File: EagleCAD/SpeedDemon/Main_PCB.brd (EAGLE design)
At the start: 77 x 46.5 mm, 71 parts, among them Q1 DMC2700, U3 LM3676, U4 STM32F072-LQFP48, X1 32.768kHz

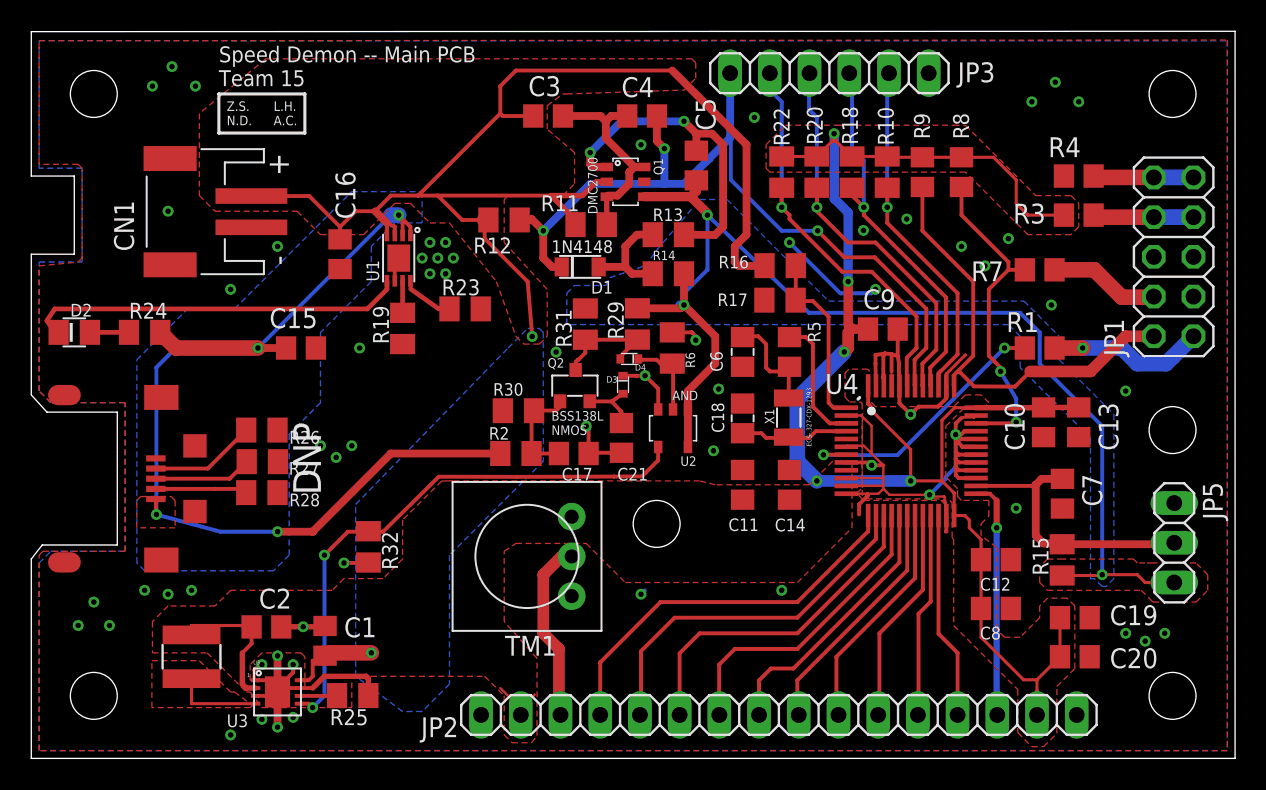
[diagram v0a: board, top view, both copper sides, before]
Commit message: added 8MHz oscillator citcuit to layout and schematic
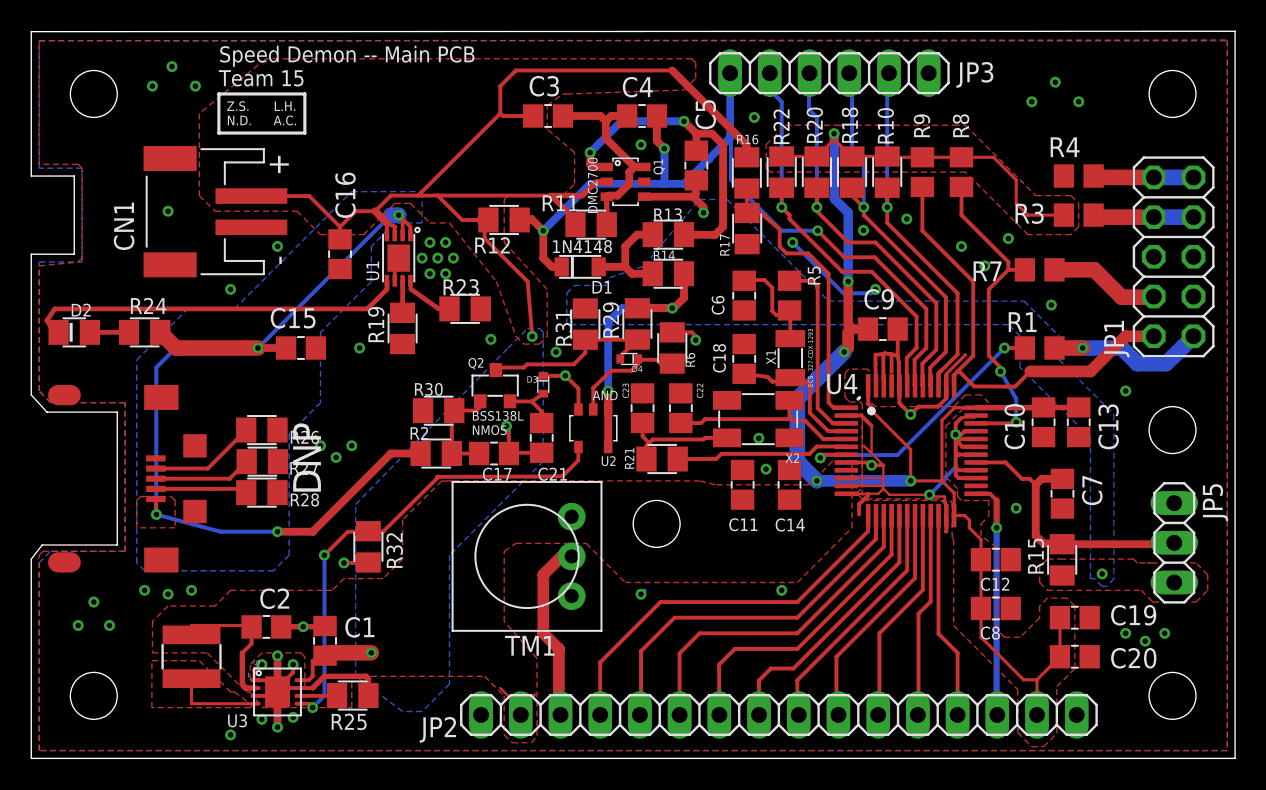
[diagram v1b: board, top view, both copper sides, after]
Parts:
- added C22, C23: 22pF, LCRD_SMD_generics:C_0805
- added R21: 0, LCRD_SMD_generics:R_0805
- added X2: (no value), LCRD_SMD_generics:4-SMD
- moved R16 6.30 mm to (45.8, 37.5), turned to 90 degrees
- moved Q2 5.10 mm to (29.7, 23.8)
- moved C17 5.10 mm to (29.6, 19.5)
- moved C21 5.10 mm to (32.6, 20.5)
- moved D3 5.10 mm to (32.8, 23.9)
- moved R2 5.10 mm to (25.9, 19.5)
- moved R30 5.10 mm to (26.1, 22.2)
- moved U2 5.10 mm to (36.0, 21.1)
- moved R17 5.04 mm to (45.8, 33.9), turned to 90 degrees
- moved C18 3.80 mm to (45.6, 25.6)
- moved X1 3.80 mm to (48.5, 25.6)
- moved C6 3.60 mm to (45.6, 29.6)
- moved R5 3.60 mm to (48.5, 29.6)
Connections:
- new net N$13: R21.2, U4.6
- new net N$17: C22.2, U4.5, X2.P$01
- new net N$18: C23.2, R21.1, X2.P$03
- net GND: now also C22.1, C23.1, U4.26, X2.P$02, X2.P$04; no longer U4.29, U4.5, U4.6
- net SENSOR_SIG_OP: now also U4.29; no longer U4.26
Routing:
- net VBATT+_SW: track 76.9 -> 22.9 mm, vias 3 -> 4
- net N$17: track 0.00 -> 12.5 mm
- net N$13: track 0.00 -> 11.1 mm
- net VBATT+: track 88.7 -> 79.7 mm
- net N$18: track 0.00 -> 7.66 mm
- net N$7: track 11.5 -> 18.7 mm
- net +V+_CHG: track 65.7 -> 60.6 mm
- net BATT_CHG_LOGIC_OP: track 35.7 -> 30.8 mm
- net N$28: track 7.23 -> 12.0 mm
- net N$5: track 8.26 -> 12.0 mm
- net GND: track 105.1 -> 102.4 mm, vias 62 -> 63
- net OSC32_OUT: track 7.00 -> 9.28 mm
- net N$11: track 5.25 -> 7.50 mm
- net SENSOR_SIG_OP: track 18.1 -> 18.7 mm
- net FL_RESET: track 17.2 -> 17.8 mm

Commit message: schematic/layout detail work.
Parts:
- CONN1: device USB_jack_102-4008-1-ND:UJ2-MIBH-4-MSMT-TR -> USB_micro_jack:USB_JACK_102-4008-1-ND_UJ2-MIBH-4-MSMT-TR
- Q2: value (none) -> BSS138L
- U2: value (none) -> NC7S08M
- moved C16 0.50 mm to (19.8, 32.8)
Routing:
- net GND: track 102.4 -> 85.4 mm, vias 63 -> 60
- net +3V3: track 114.3 -> 107.4 mm
- net PWR_SW: track 52.2 -> 50.3 mm
- net VBATT+: track 79.7 -> 78.4 mm
- net +V+_CHG: track 60.6 -> 59.6 mm
- net N$19: track 12.0 -> 12.8 mm
- net N$20: track 3.91 -> 4.49 mm
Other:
- outline, holes or cut-outs redrawn
- board text added: "L1"
- board text added: "Speed Demon -- Main PCB Team 15 (Rev.1)"
- board text removed: "Speed Demon -- Main PCB Team 15"
- board text removed: "U1"
- board text removed: "U3"

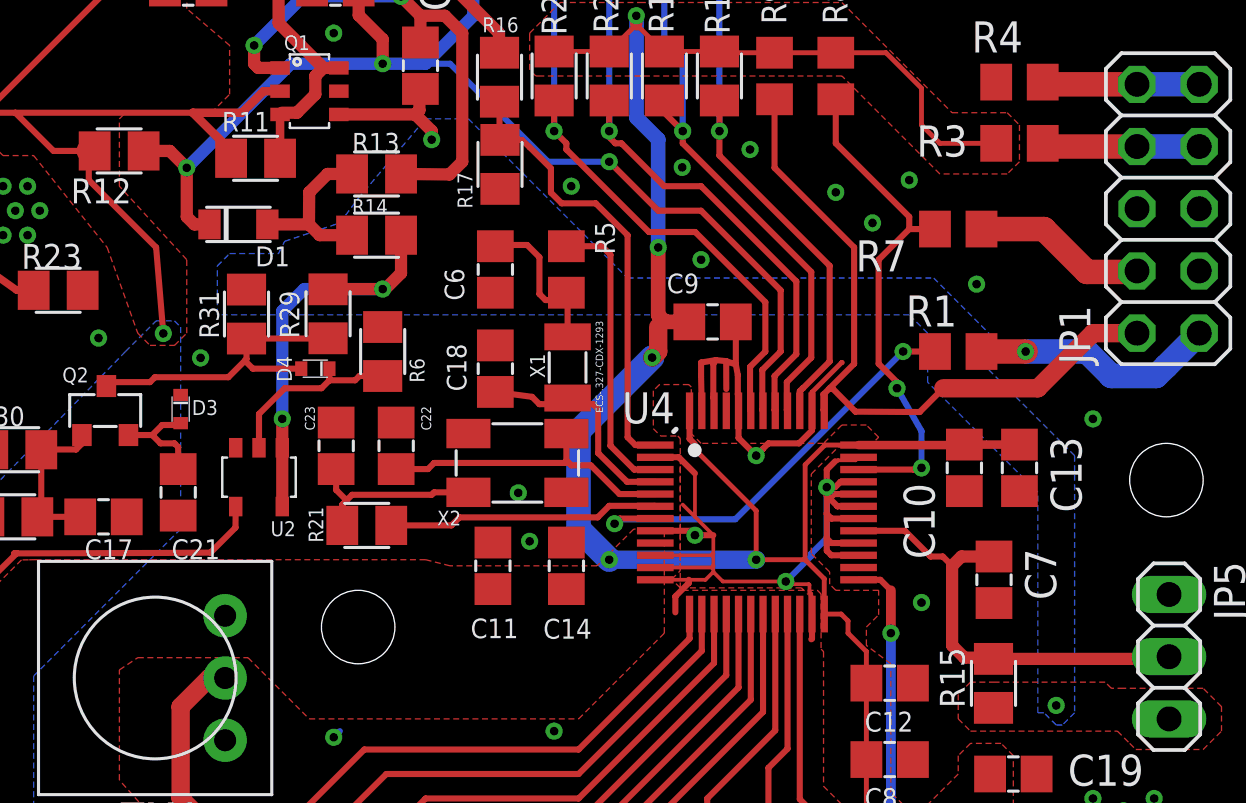
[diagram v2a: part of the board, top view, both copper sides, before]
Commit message: final changes to power defeat logic
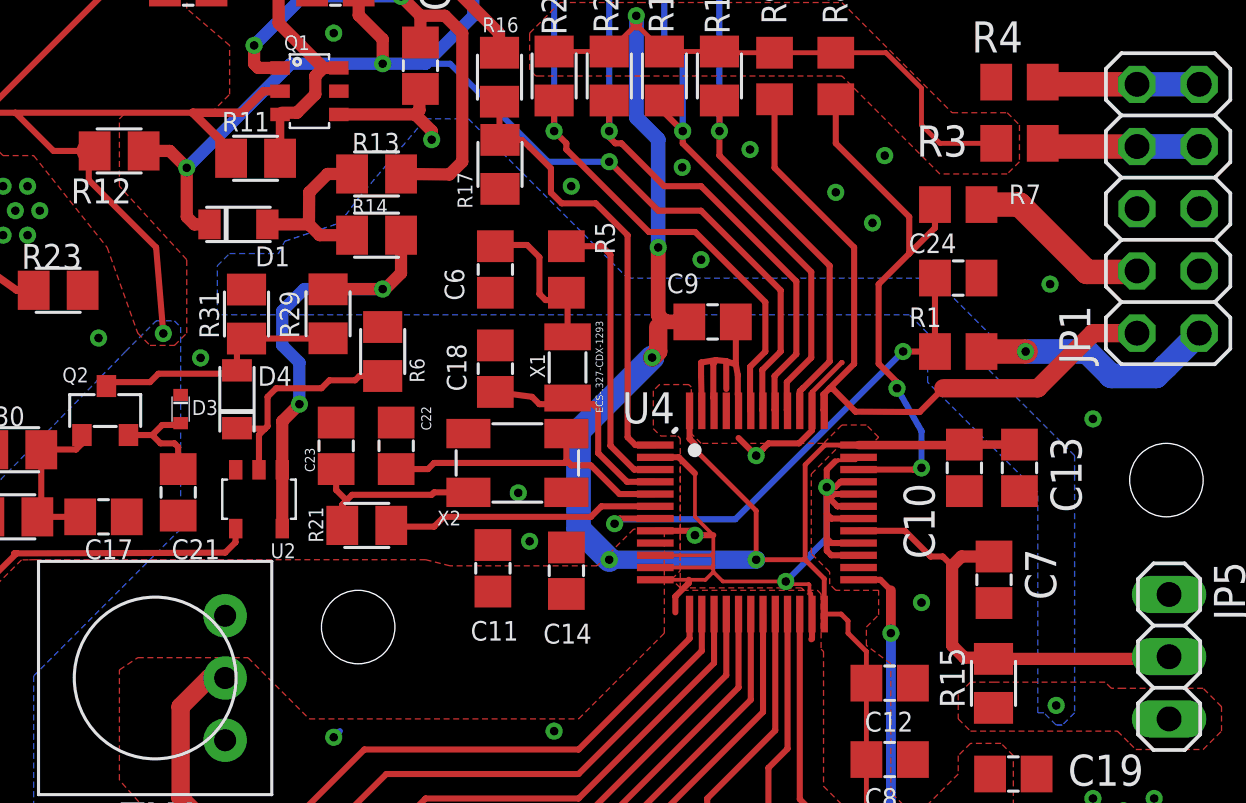
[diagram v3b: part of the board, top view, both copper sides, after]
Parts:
- added C24: 100nF, 0805_generics:C_0805
- D4: value (none) -> 1N4148; device LCRD_SMD_generics:SOD-882 -> LCRD_SMD_generics:D_SOD_123
- R31: value 1M -> DNP
- R6: value 1k -> 100k
- moved D4 3.44 mm to (35.0, 24.3), turned to 270 degrees
- moved R7 1.00 mm to (64.5, 32.2)
- moved U2 0.90 mm to (36.0, 20.2)
- moved C14 0.20 mm to (48.5, 17.3)
- moved C11 0.10 mm to (45.5, 17.4)
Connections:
- net FL_RESET: now also C24.1
- net GND: now also C24.2
- net N$11: now also D4.2; no longer D4.P$2
- net N$19: now also D4.1; no longer D4.P$1
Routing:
- net FL_RESET: track 17.8 -> 20.8 mm
- net GND: track 85.4 -> 82.9 mm
- net N$11: track 7.55 -> 9.81 mm
- net N$19: track 12.8 -> 11.2 mm
- net VBATT+_SW: track 22.9 -> 24.3 mm
- net FL_SWDIO: track 21.0 -> 22.4 mm
- net BATT_CHG_LOGIC_OP: track 30.8 -> 30.3 mm

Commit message: final layout adjustments
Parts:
- added R33: 10k, rcl:R0805
- moved CN1 1.71 mm to (12.1, 34.8)
- moved C16 0.95 mm to (20.6, 33.0)
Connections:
- net FL_SWCLK: now also R33.2
- net GND: now also R33.1
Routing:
- net +3V3: track 107.5 -> 103.5 mm
- net VBATT+: track 78.4 -> 77.2 mm
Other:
- outline, holes or cut-outs redrawn
- board text removed: "L1"

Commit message: final board
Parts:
- moved C16 12.3 mm to (10.8, 40.4), turned to 180 degrees
- moved CN1 3.50 mm to (15.6, 34.8)
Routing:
- net VBATT+: track 77.2 -> 72.8 mm
- net GND: track 82.9 -> 85.5 mm
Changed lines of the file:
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@@
 <setting verticaltext="up"/>
 </settings>
-<grid distance="1" unitdist="mm" unit="mm" style="lines" multiple="1" display="no" altdistance="0.05" altunitdist="mm" altunit="mm"/>
+<grid distance="0.25" unitdist="mm" unit="mm" style="lines" multiple="1" display="no" altdistance="0.05" altunitdist="mm" altunit="mm"/>
 <layers>
 <layer number="1" name="Top" color="4" fill="1" visible="yes" active="yes"/>
@@
 <dimension x1="78" y1="46.5" x2="78" y2="42.5" x3="78.5" y3="44.5" textsize="1.778" layer="51"/>
 <dimension x1="77" y1="0" x2="77" y2="21" x3="80" y3="10.5" textsize="1.778" layer="51"/>
-<text x="12" y="41.25" size="1.016" layer="21">Speed Demon -- Main PCB
+<text x="13" y="41.5" size="1.016" layer="21">Speed Demon -- Main PCB
 Team 15
 (Rev.1)</text>
-<text x="23.5" y="41.5" size="0.6096" layer="21">Z.S.
+<text x="25" y="41.5" size="0.6096" layer="21">Z.S.
 N.D.</text>
-<text x="26.5" y="41.5" size="0.6096" layer="21">L.H.
+<text x="28" y="41.5" size="0.6096" layer="21">L.H.
 A.C.</text>
-<wire x1="23" y1="43.5" x2="28.5" y2="43.5" width="0.2" layer="21"/>
-<wire x1="28.5" y1="43.5" x2="28.5" y2="41" width="0.2" layer="21"/>
-<wire x1="28.5" y1="41" x2="23" y2="41" width="0.2" layer="21"/>
-<wire x1="23" y1="41" x2="23" y2="43.5" width="0.2" layer="21"/>
+<wire x1="24.5" y1="43.5" x2="30" y2="43.5" width="0.2" layer="21"/>
+<wire x1="30" y1="43.5" x2="30" y2="41" width="0.2" layer="21"/>
+<wire x1="30" y1="41" x2="24.5" y2="41" width="0.2" layer="21"/>
+<wire x1="24.5" y1="41" x2="24.5" y2="43.5" width="0.2" layer="21"/>
 </plain>
 <attributes>
@@
 <attribute name="VALUE" x="15.98" y="23.71" size="1.27" layer="27"/>
 </element>
-<element name="C16" library="0805_generics" package="C_0805" value="4.7uF" x="20.65" y="33.05" smashed="yes" rot="R270">
-<attribute name="NAME" x="21.63" y="35.28" size="1.27" layer="25" rot="R90"/>
-<attribute name="VALUE" x="18.11" y="34.32" size="1.27" layer="27" rot="R270"/>
+<element name="C16" library="0805_generics" package="C_0805" value="4.7uF" x="10.8" y="40.35" smashed="yes" rot="R180">
+<attribute name="NAME" x="8.78" y="38.37" size="0.8" layer="25"/>
+<attribute name="VALUE" x="12.07" y="42.89" size="1.27" layer="27" rot="R180"/>
 </element>
 <element name="C18" library="LCRD_SMD_generics" package="C_0805" value="22pF" x="45.6" y="25.55" smashed="yes" rot="R270">
@@
 <attribute name="VALUE" x="53.2" y="24.92" size="1.27" layer="27"/>
 </element>
-<element name="CN1" library="adafruit" library_urn="urn:adsk.eagle:library:420" package="JST-PH-2-SMT-RA" value="" x="12.08" y="34.77" smashed="yes" rot="R90">
-<attribute name="NAME" x="8.67" y="30.68" size="1.27" layer="25" font="vector" rot="R90"/>
-<attribute name="VALUE" x="19.7" y="32.23" size="1.27" layer="27" font="vector" rot="R90"/>
+<element name="CN1" library="adafruit" library_urn="urn:adsk.eagle:library:420" package="JST-PH-2-SMT-RA" value="" x="15.58" y="34.77" smashed="yes" rot="R90">
+<attribute name="NAME" x="12.17" y="30.68" size="1.27" layer="25" font="vector" rot="R90"/>
+<attribute name="VALUE" x="23.2" y="32.23" size="1.27" layer="27" font="vector" rot="R90"/>
 </element>
 <element name="D1" library="LCRD_SMD_generics" package="D_SOD_123" value="1N4148_SOD_123" x="35.11" y="31.44" smashed="yes" rot="R180">
@@
 <wire x1="54.5" y1="24.36" x2="54.5" y2="25.75" width="0.25" layer="1"/>
 <wire x1="54.5" y1="25.75" x2="54.6" y2="25.9" width="0.25" layer="1"/>
-<wire x1="55.03" y1="24.72" x2="55.0263" y2="25.857084375" width="0.25" layer="1"/>
+<wire x1="55.03" y1="24.72" x2="55.028275" y2="25.250090625" width="0.25" layer="1"/>
+<wire x1="55.028275" y1="25.250090625" x2="55.0263" y2="25.857084375" width="0.25" layer="1"/>
 <wire x1="55.53" y1="24.47" x2="55.5" y2="24.5" width="0.25" layer="1"/>
 <wire x1="55.5" y1="24.5" x2="55.5" y2="25.28365" width="0.25" layer="1"/>
@@
 <wire x1="52.134565625" y1="21.934565625" x2="52.13" y2="21.93" width="0.25" layer="1"/>
 <contactref element="R33" pad="1"/>
+<wire x1="55.028275" y1="25.250090625" x2="55.028275" y2="23.831725" width="0.25" layer="1"/>
+<wire x1="55.028275" y1="23.831725" x2="55.03" y2="23.83" width="0.25" layer="1"/>
+<wire x1="55.53" y1="22.72" x2="55.53" y2="23.83" width="0.25" layer="1"/>
 </signal>
 <signal name="N$10">
@@
 <contactref element="R11" pad="2"/>
 <contactref element="R16" pad="2"/>
-<wire x1="20.75" y1="35" x2="22" y2="35" width="0.25" layer="1"/>
-<wire x1="22" y1="35" x2="22.75" y2="34.25" width="0.5" layer="1"/>
 <wire x1="22.75" y1="34.25" x2="22.75" y2="33.45" width="0.25" layer="1"/>
 <wire x1="22.75" y1="34.25" x2="23.246984375" y2="34.013325" width="0.25" layer="1"/>
-<wire x1="20.65" y1="34" x2="19.75" y2="34" width="0.25" layer="1"/>
-<wire x1="22" y1="35" x2="23" y2="36" width="0.25" layer="1"/>
 <wire x1="29" y1="34.44" x2="27.56" y2="34.44" width="0.25" layer="1"/>
 <wire x1="29" y1="34.44" x2="29.24" y2="34.44" width="1" layer="1"/>
-<wire x1="26" y1="36" x2="24.75" y2="36" width="0.25" layer="1"/>
-<wire x1="24.75" y1="36" x2="23" y2="36" width="0.25" layer="1"/>
+<wire x1="24.75" y1="36" x2="26" y2="36" width="0.25" layer="1"/>
 <wire x1="26" y1="36" x2="27.56" y2="34.44" width="0.25" layer="1"/>
 <wire x1="26" y1="36" x2="33.25" y2="36" width="0.25" layer="1"/>
@@
 <vertex x="11.75" y="35"/>
 <vertex x="19.1" y="34.9"/>
-<vertex x="19.2" y="34.8"/>
-<vertex x="19.2" y="33.7"/>
-<vertex x="19.4" y="33.5"/>
-<vertex x="21.25" y="33.5"/>
-<vertex x="23.25" y="35.5"/>
+<vertex x="22.3" y="34.9"/>
+<vertex x="22.85" y="35.5"/>
 <vertex x="24.25" y="35.5"/>
 <vertex x="25.5" y="34.25"/>
@@
 <wire x1="45.75" y1="39.25" x2="45.75" y2="39.07" width="0.5" layer="1"/>
 <wire x1="45.75" y1="39.07" x2="45.77" y2="38.45" width="0.5" layer="1"/>
-<wire x1="19.98" y1="35.77" x2="20.75" y2="35" width="0.25" layer="1"/>
-<wire x1="15.78" y1="35.77" x2="19.98" y2="35.77" width="0.25" layer="1"/>
+<wire x1="19.28" y1="35.77" x2="22.27" y2="35.77" width="0.25" layer="1"/>
+<wire x1="22.27" y1="35.77" x2="22.5" y2="36" width="0.25" layer="1"/>
+<wire x1="22.5" y1="36" x2="24.75" y2="36" width="0.25" layer="1"/>
+<wire x1="22.27" y1="35.77" x2="22.27" y2="34.73" width="0.25" layer="1"/>
+<wire x1="22.27" y1="34.73" x2="22.75" y2="34.25" width="0.25" layer="1"/>
 </signal>
 <signal name="OSC32_OUT">
